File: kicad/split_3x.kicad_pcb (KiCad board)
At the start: 2 copper layers, 127.3 x 121.2 mm, 73 parts, among them SW1 SW_Push, SW2 SW_Push, SW3 Rotary_Encoder_Switch, SW4 Rotary_Encoder_Switch, U1 ProMicro, U2 TRRS

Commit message: added pictures
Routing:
- net ground: track 236.9 -> 248.6 mm, vias 27 -> 29

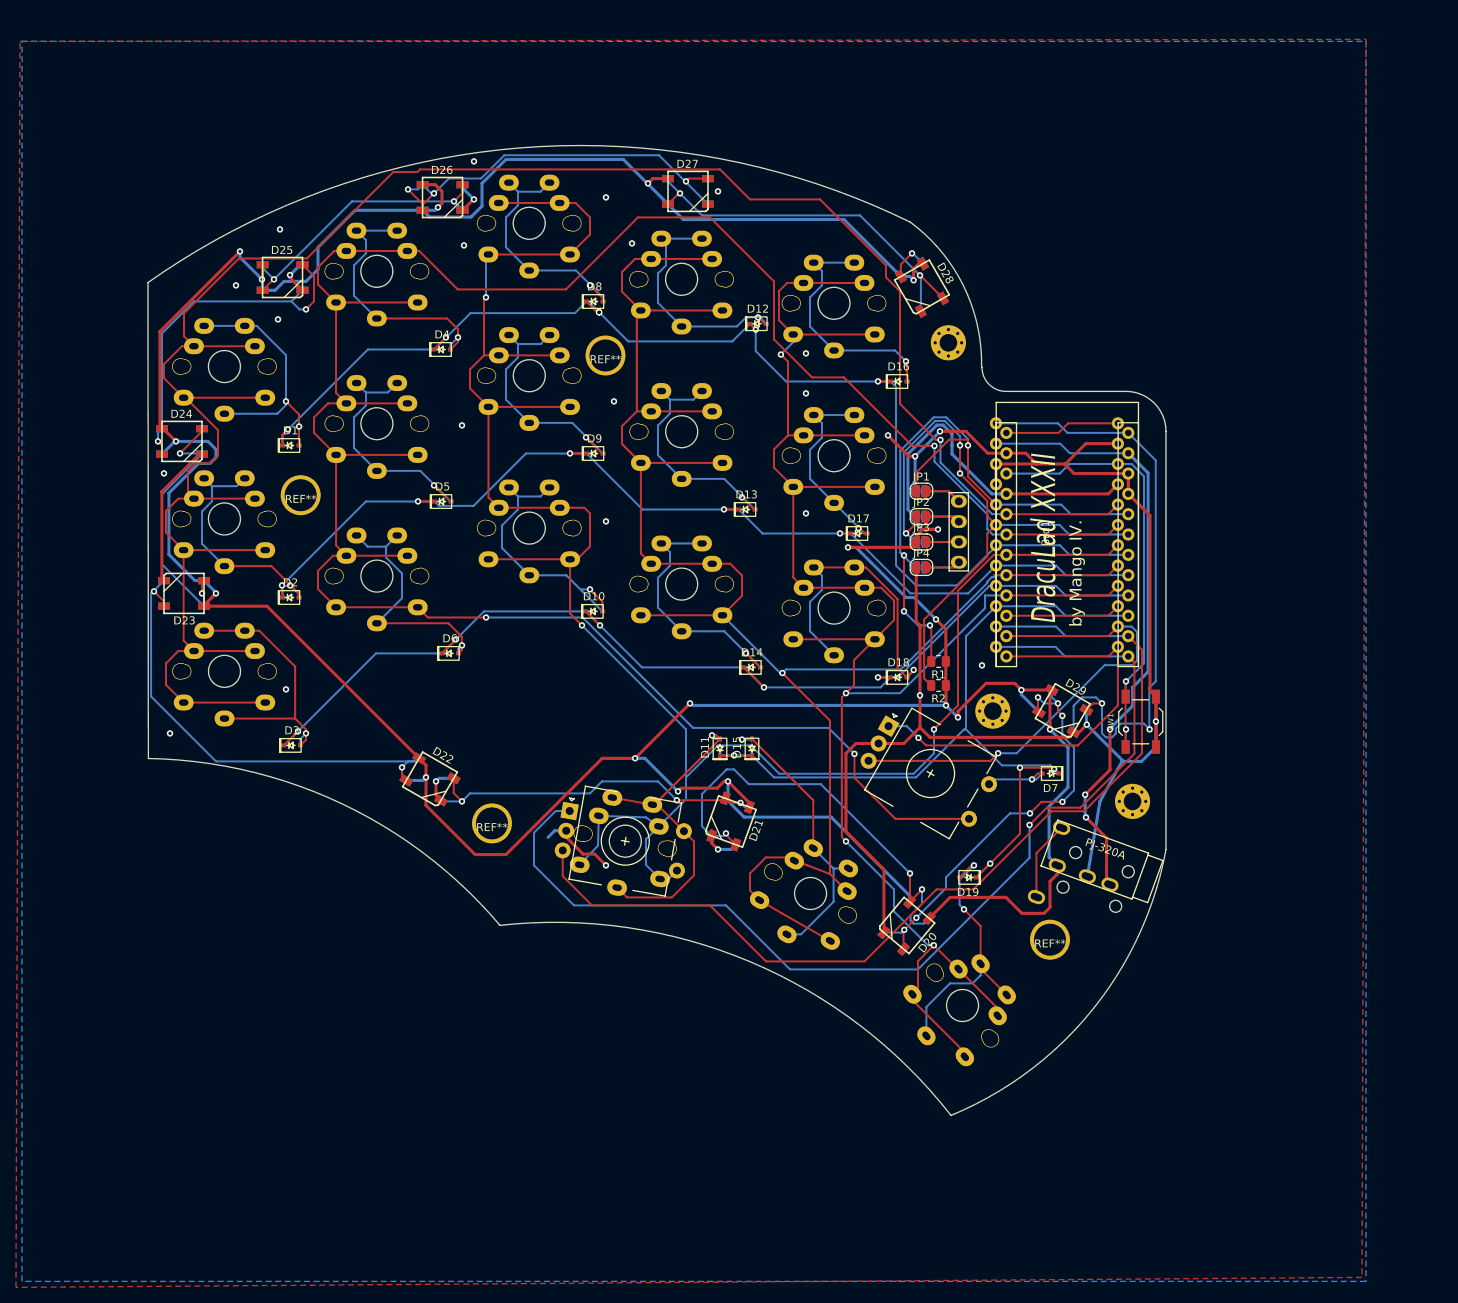
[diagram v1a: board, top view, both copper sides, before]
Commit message: added support for the pimoroni trackball breakout, changed a bunch of things, rewired the pcb, changed the bottom plate to be prettier, added some silkscreen, changed the position of one of the mounting holes, changed the angle of the trrs jacks to be properly aligned, changed the top plate to look better
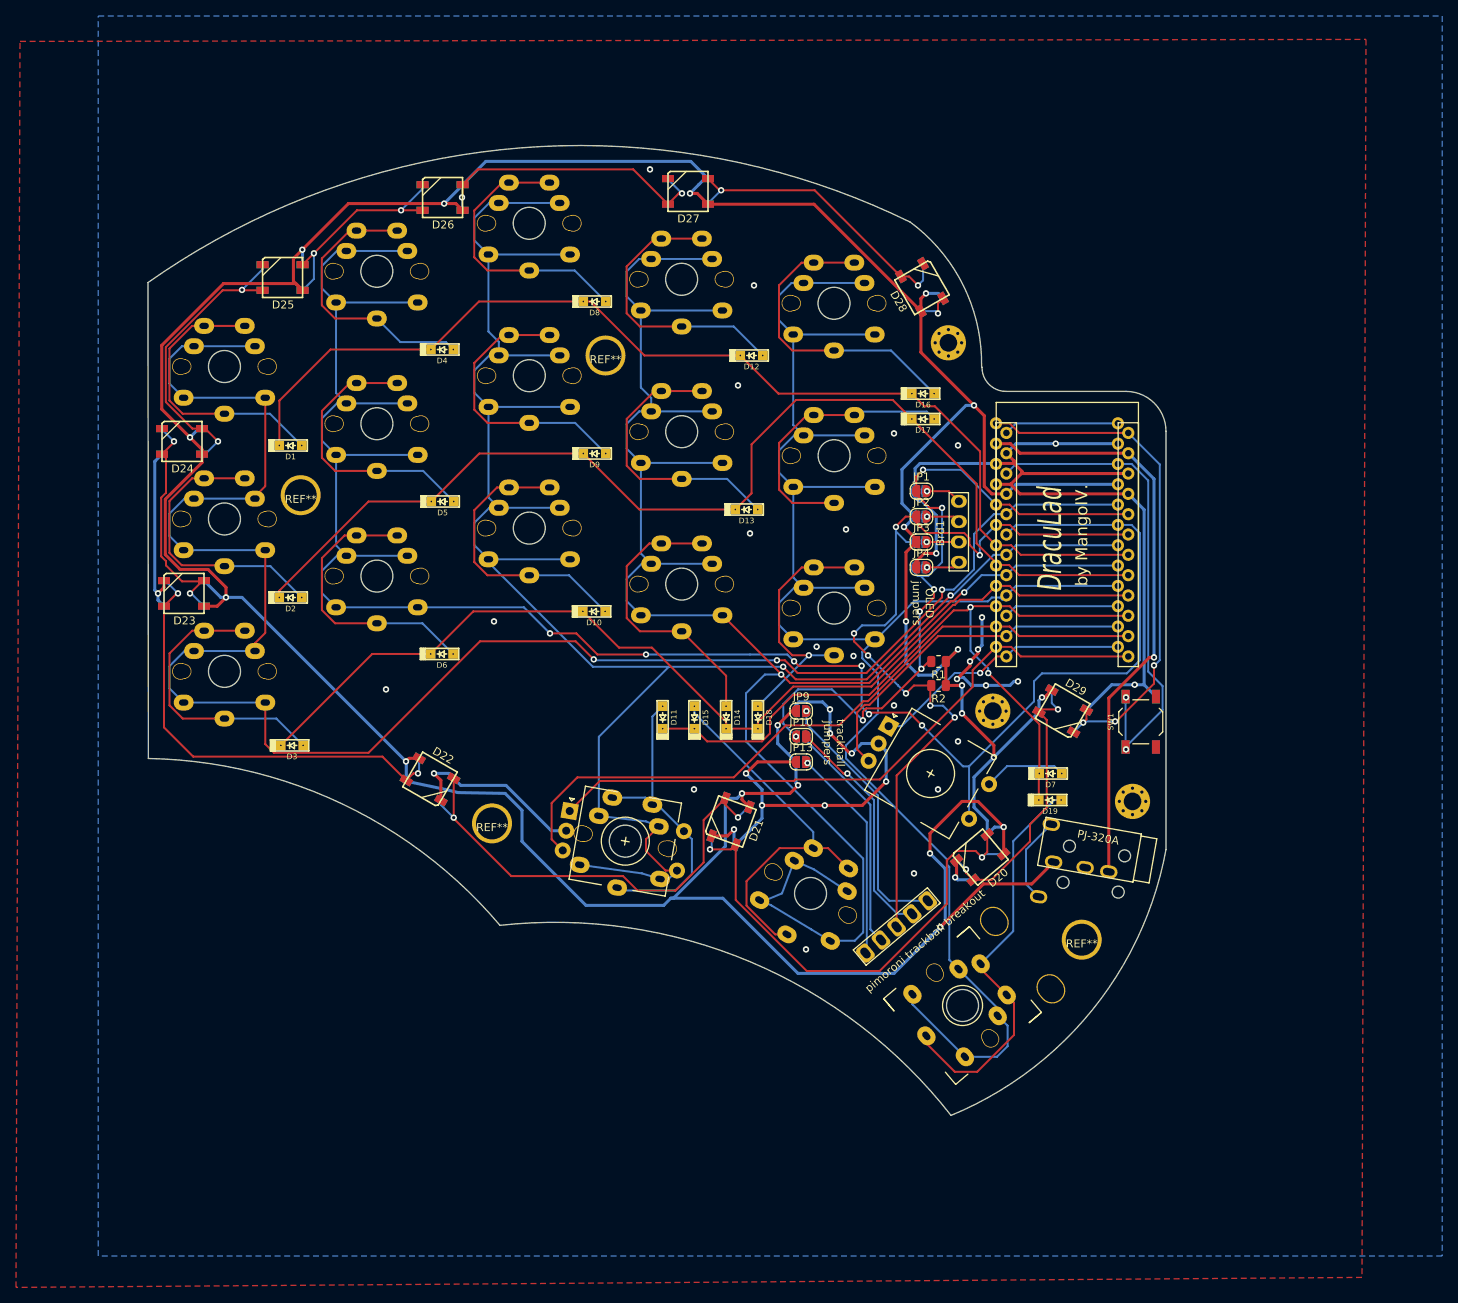
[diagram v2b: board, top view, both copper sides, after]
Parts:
- added JP10: Jumper_NO_Small, Jumper:SolderJumper-2_P1.3mm_Open_RoundedPad1.0x1.5mm, F.Cu at (159.4, 115.9)
- added JP13: Jumper_NO_Small, Jumper:SolderJumper-2_P1.3mm_Open_RoundedPad1.0x1.5mm, F.Cu at (159.4, 119.1)
- added JP14: Jumper_NO_Small, Jumper:SolderJumper-2_P1.3mm_Open_RoundedPad1.0x1.5mm, B.Cu at (159.4, 119.1)
- added JP15: Jumper_NO_Small, Jumper:SolderJumper-2_P1.3mm_Open_RoundedPad1.0x1.5mm, B.Cu at (159.4, 115.9)
- added JP18: Jumper_NO_Small, Jumper:SolderJumper-2_P1.3mm_Open_RoundedPad1.0x1.5mm, B.Cu at (159.4, 112.7)
- added JP9: Jumper_NO_Small, Jumper:SolderJumper-2_P1.3mm_Open_RoundedPad1.0x1.5mm, F.Cu at (159.4, 112.7)
- added spi1: Conn_01x05, other_parts:pimoroni_left_side_mount, B.Cu at (179.6, 149.5)
- D1, D10, D11, D12, D13, D14, D15, D16, D17, D18, D19, D2, D3, D4, D5, D6, D7, D8, D9: footprint Keebio-Parts:D_SOD-323 -> Keebio-Parts:D_SOD123F
- moved D18 18.3 mm to (154.0, 113.5), turned to 90 degrees
- moved D17 16.4 mm to (174.6, 76.2)
- moved D19 14.1 mm to (190.5, 123.8), turned to 0 degrees
- moved D20 12.6 mm to (181.8, 131.0), turned to 220 degrees
- moved D15 8.12 mm to (146.1, 113.5)
- moved D11 8.09 mm to (142.1, 113.5)
- moved D14 7.04 mm to (150.0, 113.5), turned to 90 degrees
- moved D12 4.05 mm to (153.2, 68.3)
- moved REF** 3.97 mm to (194.5, 141.3)
- moved D16 3.41 mm to (174.6, 73.0)
- moved U2 2.15 mm to (201.0, 133.3), turned to 260 degrees
- moved D6 1.01 mm to (114.5, 105.6)
- turned D24 to 180 degrees
- turned D25 to 180 degrees
- turned D26 to 180 degrees
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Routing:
- net col1: track 309.5 -> 255.9 mm, vias 3 -> 6
- net enc1db: track 133.2 -> 80.0 mm, vias 1 -> 0
- net enc1da: track 123.2 -> 88.2 mm
- net col0: track 271.7 -> 238.9 mm, vias 1 -> 3
- net Net-(JP18-Pad2): track 0.00 -> 32.8 mm, vias 0 -> 1
- net Net-(JP15-Pad2): track 0.00 -> 29.3 mm
- net Net-(JP10-Pad2): track 0.00 -> 29.0 mm, vias 0 -> 1
- net Net-(JP13-Pad2): track 0.00 -> 27.1 mm, vias 0 -> 1
- net scl: track 78.0 -> 104.9 mm, vias 3 -> 7
- net row0: track 157.1 -> 135.7 mm, vias 6 -> 0
- net enc0db: track 53.5 -> 32.8 mm
- net Net-(D20-Pad4): track 52.8 -> 35.1 mm, vias 7 -> 2
- net enc0da: track 59.4 -> 43.7 mm, vias 1 -> 0
- net Net-(D19-Pad2): track 35.4 -> 51.0 mm, vias 2 -> 0
- net Net-(D26-Pad2): track 51.7 -> 36.4 mm, vias 3 -> 2
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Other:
- board text added: "DracuLad"
- board text added: "OLED jumpers"
- board text added: "by MangoIV."
- board text added: "trackball jumpers"
- board text removed: "DracuLad XXXII"
- board text removed: "by Mango IV."

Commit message: generated gerbers for the second run
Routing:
- net col0: track 238.9 -> 240.2 mm
- net ground: vias 37 -> 39
